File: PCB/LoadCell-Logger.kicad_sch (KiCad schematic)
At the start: 72 parts, among them CN1 LoadCell, CN2 LoadCell, CN3 LoadCell, CN4 LoadCell, J1 Debug, J2 Debug_Power, J3 Debug_XH, Q1 MMBT3906, Q2 MMBT3906, Q3 MMBT3906, Q4 MMBT3906, SW3 Reset, SW4 SW_SPDT, U1 Pico, U2 TC74HCU04AF, U3 HX711, U4 HX711, U5 HX711, U6 HX711, U7 Pico, Y1 13.824MHz

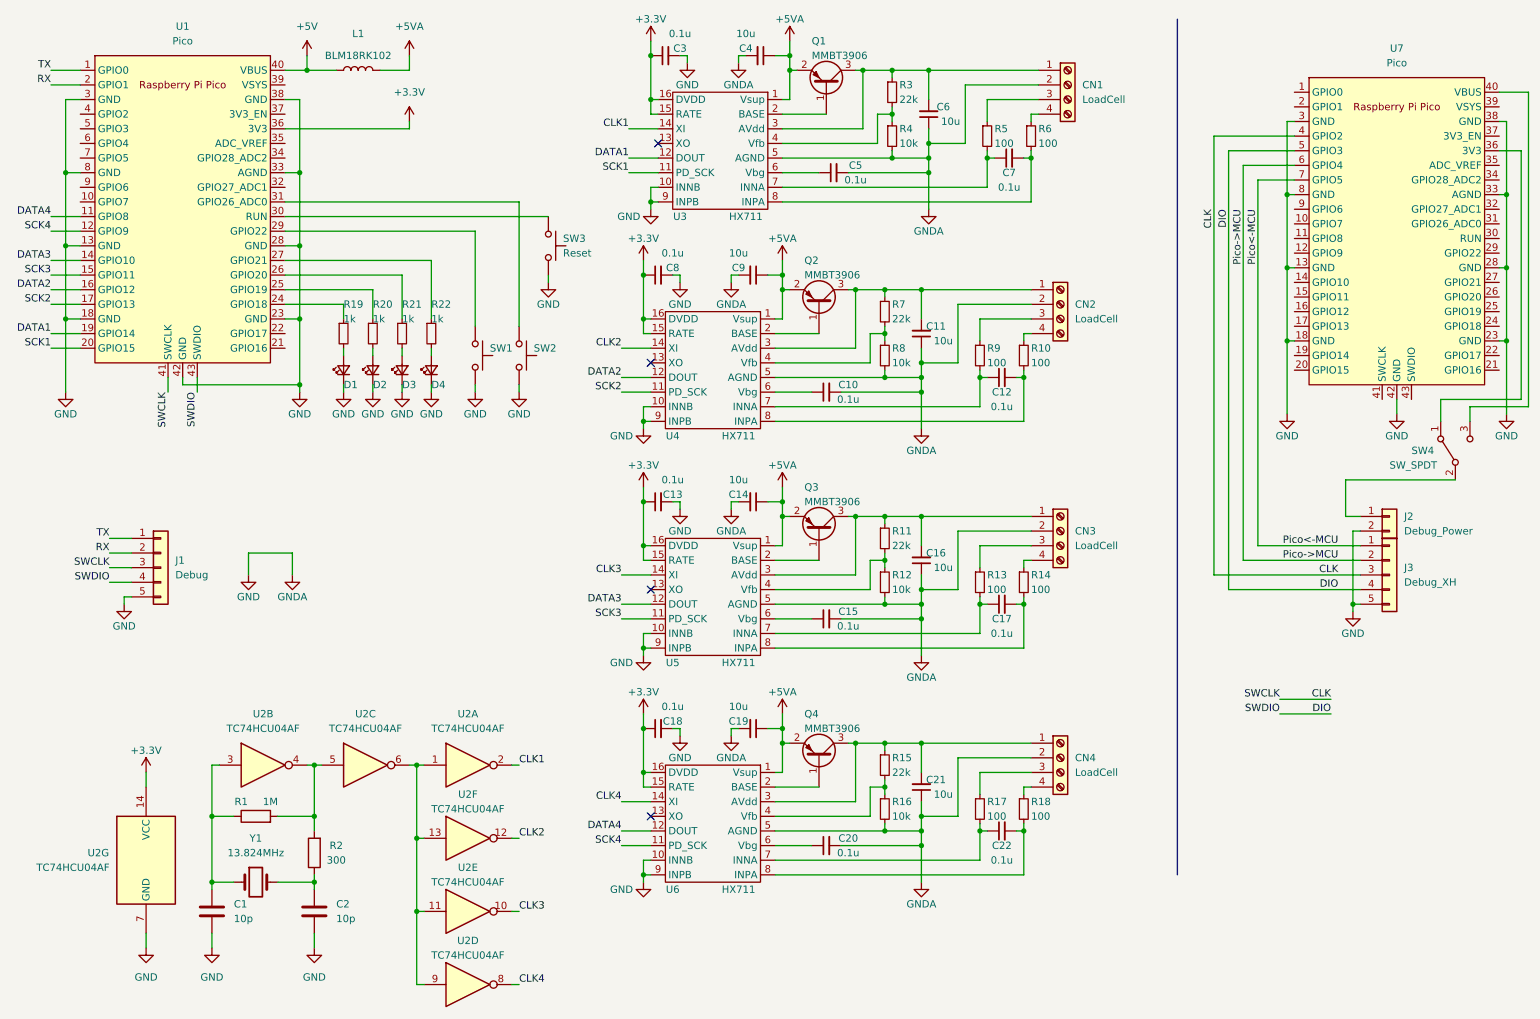
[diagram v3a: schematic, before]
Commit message: デバッガー削除
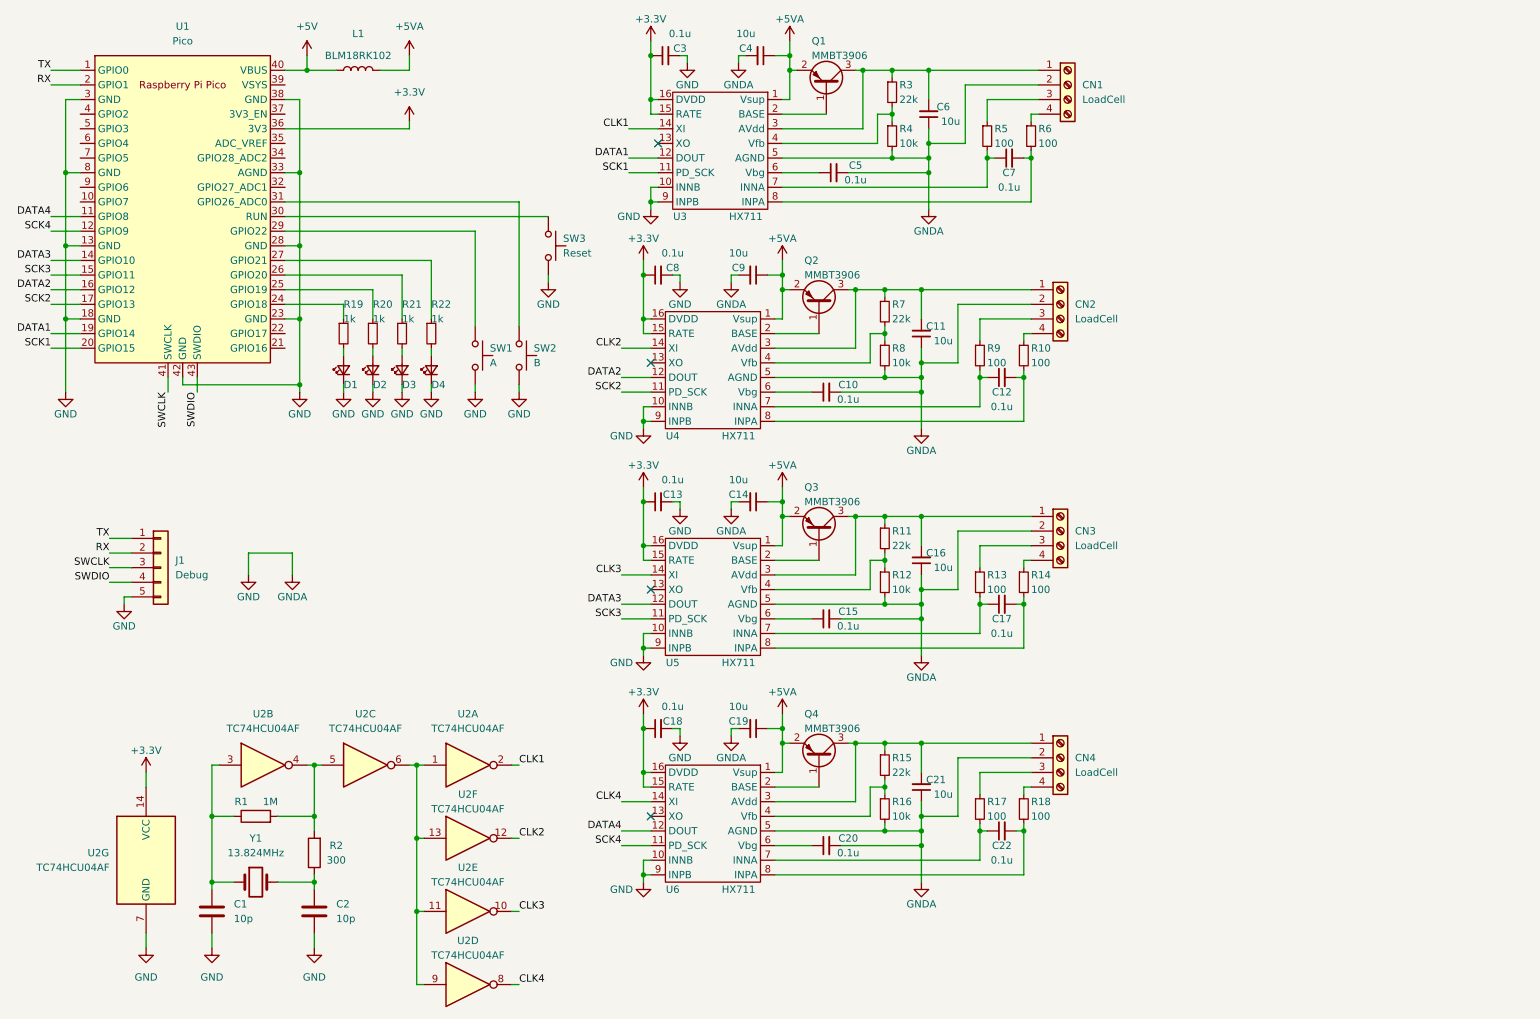
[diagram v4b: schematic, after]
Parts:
- removed J2: Debug_Power, Connector_JST:JST_XH_S2B-XH-A_1x02_P2.50mm_Horizontal, symbol Connector_Generic:Conn_01x02
- removed J3: Debug_XH, Connector_JST:JST_XH_S5B-XH-A_1x05_P2.50mm_Horizontal, symbol Connector_Generic:Conn_01x05
- removed SW4: SW_SPDT, user:SSSS213202_parallel, symbol Switch:SW_SPDT
- removed U7: Pico, MCU_RaspberryPi_and_Boards:RPi_Pico_SMD_TH, symbol MCU_RaspberryPi_and_Boards:Pico
- SW1: value (none) -> A
- SW2: value (none) -> B
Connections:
- net CLK renamed SWCLK
- net DIO renamed SWDIO
